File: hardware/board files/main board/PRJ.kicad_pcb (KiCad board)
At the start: 4 copper layers, 30 x 29.2 mm, 24 parts, among them J1 Strain Gauge, J2 Programmer, J3 KLIPPER, U1 HX717, U2 ATtiny202-SS, U3 AMS1117-3.3

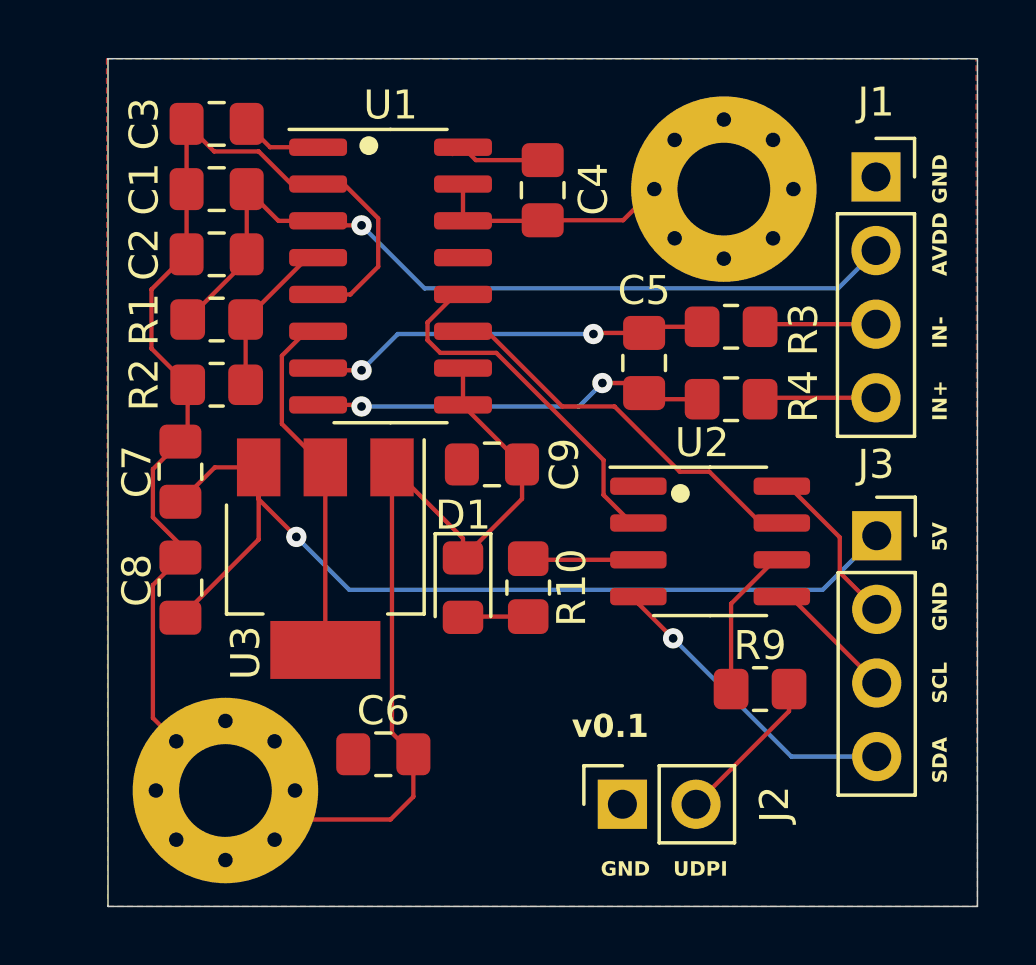
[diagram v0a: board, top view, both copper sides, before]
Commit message: first revision of on board firmware, separate hardware and software folders
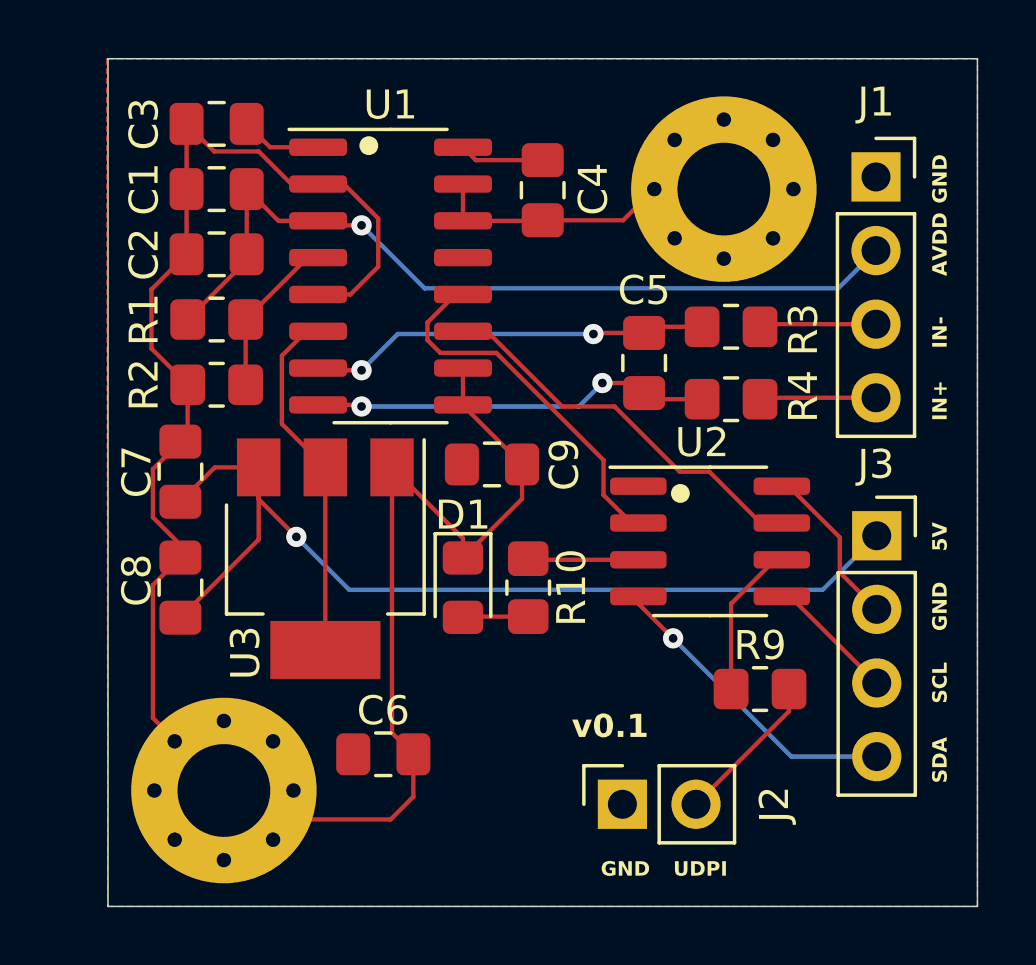
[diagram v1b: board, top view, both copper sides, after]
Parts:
- moved H1 0.05 mm to (108.5, 112.8)
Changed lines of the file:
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@@
   )
   (footprint "MountingHole:MountingHole_3.2mm_M3_Pad_Via" (layer "F.Cu")
-    (at 108.552944 112.75)
+    (at 108.5 112.75)
     (descr "Mounting Hole 3.2mm, M3")
     (tags "mounting hole 3.2mm m3")
@@
       (pts
         (xy 134.5 116.75)
-        (xy 134.45 87.5)
+        (xy 134.5 87.5)
         (xy 104.45 87.5)
         (xy 104.5 116.75)

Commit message: overhauled main board, updated credits
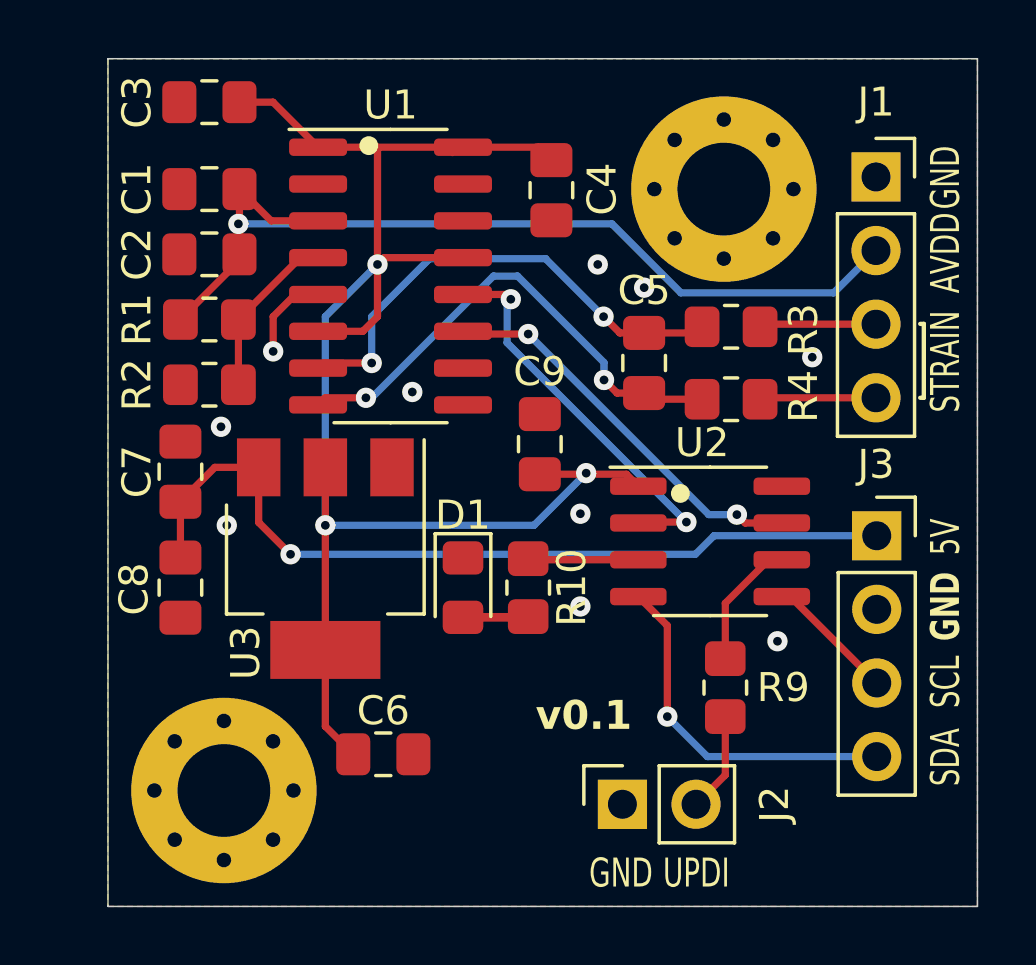
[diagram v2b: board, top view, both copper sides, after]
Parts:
- moved C9 1.79 mm to (119.4, 100.8), turned to 90 degrees
- moved R9 1.20 mm to (125.8, 109.2), turned to -90 degrees
- moved C3 0.79 mm to (108.0, 89.0)
- moved C4 0.30 mm to (119.8, 92.0)
- moved C1 0.25 mm to (108.0, 92.0)
- moved C2 0.25 mm to (108.0, 94.2)
- moved R1 0.25 mm to (108.0, 96.5)
- moved R2 0.25 mm to (108.0, 98.8)
- turned C8 to -90 degrees
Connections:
- net UDPI renamed UPDI
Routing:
- net GND: track 83.8 -> 3.42 mm, vias 0 -> 10
- net +3.3V: track 19.3 -> 57.3 mm, vias 0 -> 3
- net +5V: track 34.0 -> 29.1 mm
- net IN+: track 13.8 -> 17.5 mm
- net AVDD: track 29.0 -> 32.2 mm
- net IN-: track 13.9 -> 16.9 mm
- net UPDI: track 5.30 -> 3.44 mm
- net SDA: track 10.7 -> 12.4 mm
- net DOUT: track 12.8 -> 13.7 mm, vias 0 -> 2
- net Net-(U2-~{RESET}/PA0): track 5.32 -> 4.48 mm
- net PD_SCK: vias 0 -> 2
- added copper zone on F.Cu, net GND
- removed copper zone on F.Cu, net +3.3V
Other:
- copper layers 4 -> 2
- rule pad_to_mask_clearance: 0 -> 0.038
- board text added: "STRAIN"
- board text added: "UPDI"
- board text removed: "DEEZ"
- board text removed: "IN+"
- board text removed: "IN-"
- board text removed: "LOAD"
- board text removed: "UDPI"

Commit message: adjusted mainboard
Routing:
- net +3.3V: track 57.3 -> 55.3 mm
- net IN-: track 16.9 -> 15.9 mm
- net GND: vias 10 -> 14
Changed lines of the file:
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@@
   (via (at 120.8 103.2) (size 0.7) (drill 0.3) (layers "F.Cu" "B.Cu") (free) (net 1))
   (via (at 108.6 103.6) (size 0.7) (drill 0.3) (layers "F.Cu" "B.Cu") (free) (net 1))
+  (via (at 114.5 92) (size 0.7) (drill 0.3) (layers "F.Cu" "B.Cu") (free) (net 1))
   (via (at 120.8 106.4) (size 0.7) (drill 0.3) (layers "F.Cu" "B.Cu") (free) (net 1))
   (via (at 127.6 107.6) (size 0.7) (drill 0.3) (layers "F.Cu" "B.Cu") (free) (net 1))
-  (via (at 115 99) (size 0.7) (drill 0.3) (layers "F.Cu" "B.Cu") (free) (net 1))
-  (via (at 121.4 94.6) (size 0.7) (drill 0.3) (layers "F.Cu" "B.Cu") (free) (net 1))
+  (via (at 114.5 95.5) (size 0.7) (drill 0.3) (layers "F.Cu" "B.Cu") (free) (net 1))
   (via (at 108.4 100.2) (size 0.7) (drill 0.3) (layers "F.Cu" "B.Cu") (free) (net 1))
   (via (at 123 95.4) (size 0.7) (drill 0.3) (layers "F.Cu" "B.Cu") (free) (net 1))
+  (via (at 111 103.5) (size 0.7) (drill 0.3) (layers "F.Cu" "B.Cu") (free) (net 1))
+  (via (at 118.5 92) (size 0.7) (drill 0.3) (layers "F.Cu" "B.Cu") (free) (net 1))
   (via (at 128.8 97.8) (size 0.7) (drill 0.3) (layers "F.Cu" "B.Cu") (free) (net 1))
   (via (at 110.2 97.6) (size 0.7) (drill 0.3) (layers "F.Cu" "B.Cu") (net 1))
+  (via (at 108 90.5) (size 0.7) (drill 0.3) (layers "F.Cu" "B.Cu") (free) (net 1))
+  (via (at 125 105.5) (size 0.7) (drill 0.3) (layers "F.Cu" "B.Cu") (free) (net 1))
   (segment (start 107 102.7875) (end 108.1875 101.6) (width 0.25) (layer "F.Cu") (net 2))
   (segment (start 108.1875 101.6) (end 109.7 101.6) (width 0.25) (layer "F.Cu") (net 2))
@@
   (via (at 121.6 96.4) (size 0.7) (drill 0.3) (layers "F.Cu" "B.Cu") (net 4))
   (via (at 113.6 98) (size 0.7) (drill 0.3) (layers "F.Cu" "B.Cu") (net 4))
-  (segment (start 121.6 96.4) (end 119.6 94.4) (width 0.25) (layer "B.Cu") (net 4))
-  (segment (start 113.6 96.4) (end 113.6 98) (width 0.25) (layer "B.Cu") (net 4))
-  (segment (start 115.6 94.4) (end 113.6 96.4) (width 0.25) (layer "B.Cu") (net 4))
-  (segment (start 119.6 94.4) (end 115.6 94.4) (width 0.25) (layer "B.Cu") (net 4))
+  (segment (start 117.104 94.496) (end 113.6 98) (width 0.25) (layer "B.Cu") (net 4))
+  (segment (start 121.6 96.4) (end 119.696 94.496) (width 0.25) (layer "B.Cu") (net 4))
+  (segment (start 119.696 94.496) (end 117.104 94.496) (width 0.25) (layer "B.Cu") (net 4))
   (segment (start 125 99.25) (end 123.2125 99.25) (width 0.25) (layer "F.Cu") (net 5))
   (segment (start 123.2125 99.25) (end 123 99.0375) (width 0.25) (layer "F.Cu") (net 5))
@@
   (segment (start 118.271 95.929) (end 118.271 97.301256) (width 0.25) (layer "B.Cu") (net 12))
   (segment (start 118.4 95.8) (end 118.271 95.929) (width 0.25) (layer "B.Cu") (net 12))
-  (segment (start 113.295 96.905) (end 111.75 96.905) (width 0.25) (layer "F.Cu") (net 13))
   (segment (start 122.3875 101.8375) (end 122.8 102.25) (width 0.25) (layer "F.Cu") (net 13))
-  (segment (start 113.8 94.6) (end 113.8 96.4) (width 0.25) (layer "F.Cu") (net 13))
+  (segment (start 116.75 94.365) (end 113.635 94.365) (width 0.25) (layer "F.Cu") (net 13))
   (segment (start 112 101.6) (end 112 103.6) (width 0.25) (layer "F.Cu") (net 13))
-  (segment (start 113.8 96.4) (end 113.295 96.905) (width 0.25) (layer "F.Cu") (net 13))
   (segment (start 109.0375 89) (end 110.195 89) (width 0.25) (layer "F.Cu") (net 13))
-  (segment (start 116.75 94.365) (end 114.035 94.365) (width 0.25) (layer "F.Cu") (net 13))
   (segment (start 119.4 101.8375) (end 120.9625 101.8375) (width 0.25) (layer "F.Cu") (net 13))
   (segment (start 112 107.9) (end 112 110.5375) (width 0.25) (layer "F.Cu") (net 13))
+  (segment (start 113.5 90.555) (end 111.75 90.555) (width 0.25) (layer "F.Cu") (net 13))
+  (segment (start 113.635 94.365) (end 113.5 94.5) (width 0.25) (layer "F.Cu") (net 13))
+  (segment (start 113.8 90.555) (end 113.5 90.555) (width 0.25) (layer "F.Cu") (net 13))
+  (segment (start 113.095 96.905) (end 113.5 96.5) (width 0.25) (layer "F.Cu") (net 13))
   (segment (start 112 103.6) (end 112 107.9) (width 0.25) (layer "F.Cu") (net 13))
   (segment (start 111.75 96.905) (end 112.595 96.905) (width 0.15) (layer "F.Cu") (net 13))
@@
   (segment (start 121 101.8) (end 121.0375 101.8375) (width 0.25) (layer "F.Cu") (net 13))
   (segment (start 116.175736 90.58) (end 116.387868 90.792132) (width 0.15) (layer "F.Cu") (net 13))
-  (segment (start 114.035 94.365) (end 113.8 94.6) (width 0.25) (layer "F.Cu") (net 13))
+  (segment (start 113.5 94.5) (end 113.5 90.555) (width 0.25) (layer "F.Cu") (net 13))
+  (segment (start 113.5 96.5) (end 113.5 94.5) (width 0.25) (layer "F.Cu") (net 13))
   (segment (start 112.0375 102) (end 112 102.0375) (width 0.15) (layer "F.Cu") (net 13))
-  (segment (start 113.8 90.555) (end 113.8 94.6) (width 0.25) (layer "F.Cu") (net 13))
   (segment (start 110.195 89) (end 111.75 90.555) (width 0.25) (layer "F.Cu") (net 13))
   (segment (start 120.9625 101.8375) (end 121 101.8) (width 0.25) (layer "F.Cu") (net 13))
   (segment (start 119.355 90.555) (end 119.8 91) (width 0.25) (layer "F.Cu") (net 13))
   (segment (start 112 110.5375) (end 112.9625 111.5) (width 0.25) (layer "F.Cu") (net 13))
-  (segment (start 113.8 90.555) (end 111.75 90.555) (width 0.25) (layer "F.Cu") (net 13))
+  (segment (start 111.75 96.905) (end 113.095 96.905) (width 0.25) (layer "F.Cu") (net 13))
   (segment (start 116.75 90.555) (end 119.355 90.555) (width 0.25) (layer "F.Cu") (net 13))
-  (via (at 113.8 94.6) (size 0.7) (drill 0.3) (layers "F.Cu" "B.Cu") (net 13))
+  (via (at 113.5 96.5) (size 0.7) (drill 0.3) (layers "F.Cu" "B.Cu") (net 13))
   (via (at 121 101.8) (size 0.7) (drill 0.3) (layers "F.Cu" "B.Cu") (net 13))
   (via (at 112 103.6) (size 0.7) (drill 0.3) (layers "F.Cu" "B.Cu") (net 13))
-  (segment (start 113.8 94.6) (end 112 96.4) (width 0.25) (layer "B.Cu") (net 13))
-  (segment (start 112 96.4) (end 112 103.6) (width 0.25) (layer "B.Cu") (net 13))
+  (segment (start 113.5 96.5) (end 112 98) (width 0.25) (layer "B.Cu") (net 13))
   (segment (start 112 103.6) (end 119.2 103.6) (width 0.25) (layer "B.Cu") (net 13))
+  (segment (start 112 98) (end 112 103.6) (width 0.25) (layer "B.Cu") (net 13))
   (segment (start 119.2 103.6) (end 121 101.8) (width 0.25) (layer "B.Cu") (net 13))
   (segment (start 128.045 106.06) (end 127.75 106.06) (width 0.25) (layer "F.Cu") (net 14))
@@
   (segment (start 118.975 106.775) (end 119 106.75) (width 0.3) (layer "F.Cu") (net 17))
   (segment (start 116.75 106.775) (end 118.975 106.775) (width 0.3) (layer "F.Cu") (net 17))
-  (zone (net 1) (net_name "GND") (layer "F.Cu") (hatch edge 0.5)
-    (connect_pads (clearance 0.3))
-    (min_thickness 0.25) (filled_areas_thickness no)
-    (fill yes (thermal_gap 0.5) (thermal_bridge_width 0.5))
+  (zone (net 1) (net_name "GND") (layers "F&B.Cu") (hatch edge 0.5)
+    (connect_pads (clearance 0.2))
+    (min_thickness 0.2) (filled_areas_thickness no)
+    (fill yes (thermal_gap 0.2) (thermal_bridge_width 0.65))
     (polygon
       (pts
@@
       )
     )
-  )
-  (zone (net 1) (net_name "GND") (layer "B.Cu") (hatch edge 0.5)
-    (priority 1)
-    (connect_pads (clearance 0.3))
-    (min_thickness 0.25) (filled_areas_thickness no)
-    (fill yes (thermal_gap 0.5) (thermal_bridge_width 0.5))
-    (polygon
-      (pts
-        (xy 134.5 87.5)
-        (xy 104.5 87.5)
-        (xy 104.5 116.75)
-        (xy 134.5 116.75)
-      )
-    )

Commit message: finalized boards for production
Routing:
- net GND: track 3.42 -> 0.35 mm
- net +5V: track 29.1 -> 31.9 mm
- net DOUT: track 13.7 -> 14.0 mm, vias 2 -> 0
